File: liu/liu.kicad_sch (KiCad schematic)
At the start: 12 parts, among them J1 Screw Termial, J2 Screw Terminal, J5 I2C, J6 RotaryEncoder, U1 VoltageRegulator, U2 ESP32, U3 TJA1050

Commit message: added stuff
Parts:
- added D2: D, Resistor_THT:R_Axial_DIN0207_L6.3mm_D2.5mm_P10.16mm_Horizontal, symbol Device:D
- added R5: ~, Resistor_THT:R_Axial_DIN0207_L6.3mm_D2.5mm_P10.16mm_Horizontal, symbol Device:R
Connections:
- net 5V: now also D2.1 (K); no longer U1.4 (Pin_4)
- net at U2.1 (Pin_1): now also R5.1; no longer U3.2 (Pin_2)
- new net: D2.2 (A), U1.4 (Pin_4)
- new net: R5.2, U3.2 (Pin_2)

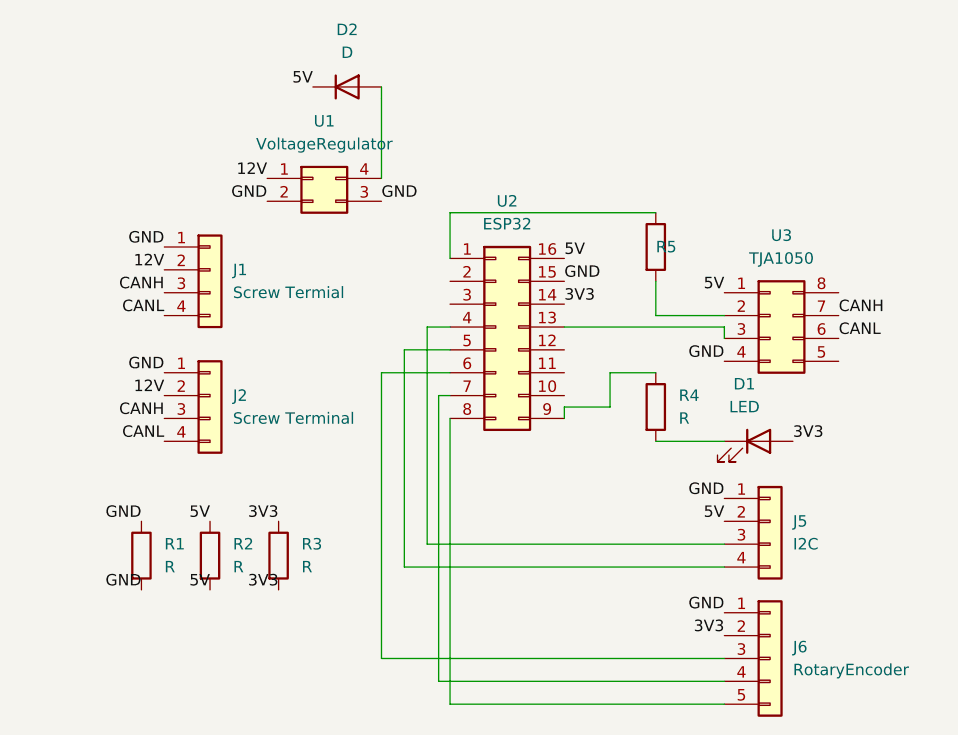
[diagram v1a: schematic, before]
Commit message: 4 screw terminals
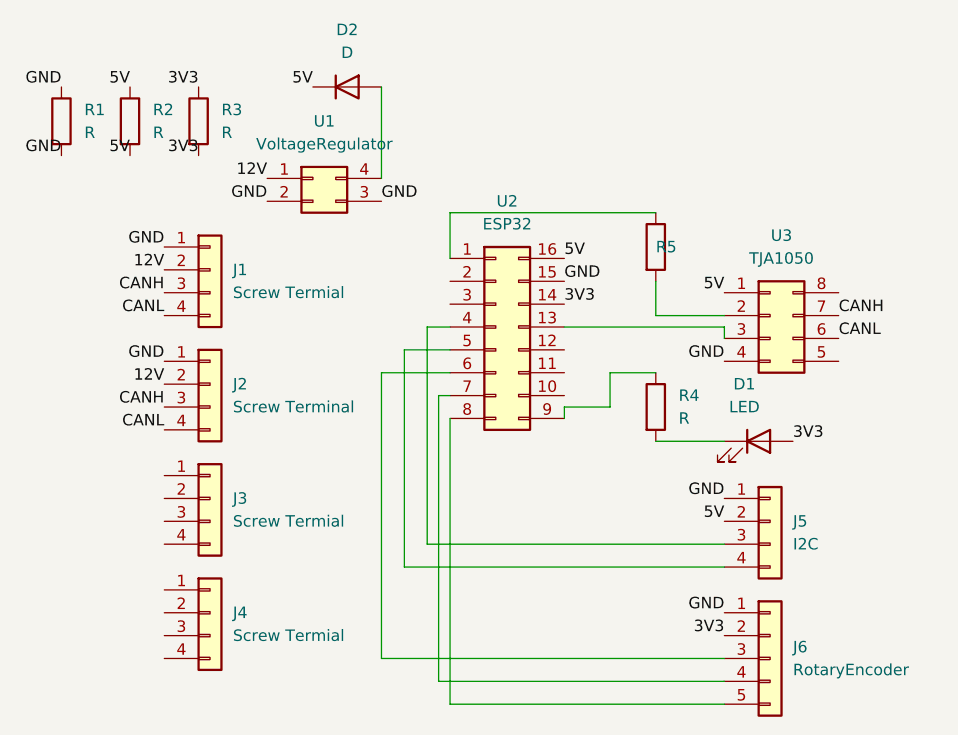
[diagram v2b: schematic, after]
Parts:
- added J3, J4: Screw Termial, Peabrain:ScrewTerminals_4P, symbol Connector_Generic:Conn_01x04
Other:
- moved on the sheet: J2, R1, R2, R3
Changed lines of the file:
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@@
+  (wire
+    (pts
+      (xy 78.74 27.94)
+      (xy 78.74 38.1)
+    )
+    (stroke
+      (width 0)
+      (type default)
+    )
+  )
   (wire
     (pts
@@
   )
   (label "5V"
-    (at 59.69 83.82 180)
+    (at 50.8 35.56 180)
     (effects
       (font
@@
   )
   (label "GND"
-    (at 52.07 83.82 180)
+    (at 43.18 35.56 180)
     (effects
       (font
@@
   )
   (label "CANL"
-    (at 54.61 67.31 180)
+    (at 54.61 66.04 180)
     (effects
       (font
@@
   )
   (label "3V3"
-    (at 67.31 83.82 180)
+    (at 58.42 35.56 180)
     (effects
       (font
@@
   )
   (label "12V"
-    (at 54.61 62.23 180)
+    (at 54.61 60.96 180)
     (effects
       (font
@@
   )
   (label "3V3"
-    (at 67.31 76.2 180)
+    (at 58.42 27.94 180)
     (effects
       (font
@@
   )
   (label "5V"
-    (at 59.69 76.2 180)
+    (at 50.8 27.94 180)
     (effects
       (font
@@
   )
   (label "GND"
-    (at 54.61 59.69 180)
+    (at 54.61 58.42 180)
     (effects
       (font
@@
   )
   (label "GND"
-    (at 52.07 76.2 180)
+    (at 43.18 27.94 180)
     (effects
       (font
@@
   )
   (label "CANH"
-    (at 54.61 64.77 180)
+    (at 54.61 63.5 180)
     (effects
       (font
@@
   (symbol
     (lib_id "Device:R")
-    (at 52.07 80.01 0)
+    (at 43.18 31.75 0)
     (unit 1)
     (exclude_from_sim no)
@@
     (fields_autoplaced yes)
     (property "Reference" "R1"
-      (at 54.61 78.7399 0)
+      (at 45.72 30.4799 0)
       (effects
         (font
@@
     )
     (property "Value" "R"
-      (at 54.61 81.2799 0)
+      (at 45.72 33.0199 0)
       (effects
         (font
@@
     )
     (property "Footprint" "Resistor_THT:R_Axial_DIN0207_L6.3mm_D2.5mm_P10.16mm_Horizontal"
-      (at 50.292 80.01 90)
+      (at 41.402 31.75 90)
       (effects
         (font
@@
     )
     (property "Datasheet" "~"
-      (at 52.07 80.01 0)
+      (at 43.18 31.75 0)
       (effects
         (font
@@
     )
     (property "Description" "Resistor"
-      (at 52.07 80.01 0)
+      (at 43.18 31.75 0)
       (effects
         (font
@@
   (symbol
     (lib_id "Device:R")
-    (at 59.69 80.01 0)
+    (at 50.8 31.75 0)
     (unit 1)
     (exclude_from_sim no)
@@
     (fields_autoplaced yes)
     (property "Reference" "R2"
-      (at 62.23 78.7399 0)
+      (at 53.34 30.4799 0)
       (effects
         (font
@@
     )
     (property "Value" "R"
-      (at 62.23 81.2799 0)
+      (at 53.34 33.0199 0)
       (effects
         (font
@@
     )
     (property "Footprint" "Resistor_THT:R_Axial_DIN0207_L6.3mm_D2.5mm_P10.16mm_Horizontal"
-      (at 57.912 80.01 90)
+      (at 49.022 31.75 90)
       (effects
         (font
@@
     )
     (property "Datasheet" "~"
-      (at 59.69 80.01 0)
+      (at 50.8 31.75 0)
       (effects
         (font
@@
     )
     (property "Description" "Resistor"
-      (at 59.69 80.01 0)
+      (at 50.8 31.75 0)
       (effects
         (font
@@
   (symbol
     (lib_id "Connector_Generic:Conn_01x04")
-    (at 59.69 62.23 0)
+    (at 59.69 73.66 0)
+    (unit 1)
+    (exclude_from_sim no)
+    (in_bom yes)
+    (on_board yes)
+    (dnp no)
+    (fields_autoplaced yes)
+    (property "Reference" "J3"
+      (at 62.23 73.6599 0)
+      (effects
+        (font
+          (size 1.27 1.27)
+        )
+        (justify left)
+      )
+    )
+    (property "Value" "Screw Termial"
+      (at 62.23 76.1999 0)
+      (effects
+        (font
+          (size 1.27 1.27)
+        )
+        (justify left)
+      )
+    )
+    (property "Footprint" "Peabrain:ScrewTerminals_4P"
+      (at 59.69 73.66 0)
+      (effects
+        (font
+          (size 1.27 1.27)
+        )
+        (hide yes)
+      )
+    )
+    (property "Datasheet" "~"
+      (at 59.69 73.66 0)
+      (effects
+        (font
+          (size 1.27 1.27)
+        )
+        (hide yes)
+      )
+    )
+    (property "Description" "Generic connector, single row, 01x04, script generated (kicad-library-utils/schlib/autogen/connector/)"
+      (at 59.69 73.66 0)
+      (effects
+        (font
+          (size 1.27 1.27)
+        )
+        (hide yes)
+      )
+    )
+    (pin "3"
+    )
+    (pin "2"
+    )
+    (pin "1"
+    )
+    (pin "4"
+    )
+    (instances
+      (project "liu"
+        (path "/94a9126b-1049-4434-a6c7-ce4492ba55c0"
+          (reference "J3")
+          (unit 1)
+        )
+      )
+    )
+  )
+  (symbol
+    (lib_id "Connector_Generic:Conn_01x04")
+    (at 59.69 60.96 0)
     (unit 1)
     (exclude_from_sim no)
@@
     (fields_autoplaced yes)
     (property "Reference" "J2"
-      (at 62.23 62.2299 0)
+      (at 62.23 60.9599 0)
       (effects
         (font
@@
     )
     (property "Value" "Screw Terminal"
-      (at 62.23 64.7699 0)
+      (at 62.23 63.4999 0)
       (effects
         (font
@@
     )
     (property "Footprint" "Peabrain:ScrewTerminals_4P"
-      (at 59.69 62.23 0)
+      (at 59.69 60.96 0)
       (effects
         (font
@@
     )
     (property "Datasheet" "~"
-      (at 59.69 62.23 0)
+      (at 59.69 60.96 0)
       (effects
         (font
@@
     )
     (property "Description" "Generic connector, single row, 01x04, script generated (kicad-library-utils/schlib/autogen/connector/)"
-      (at 59.69 62.23 0)
+      (at 59.69 60.96 0)
       (effects
         (font
@@
   )
   (symbol
+    (lib_id "Connector_Generic:Conn_01x04")
+    (at 59.69 86.36 0)
+    (unit 1)
+    (exclude_from_sim no)
+    (in_bom yes)
+    (on_board yes)
+    (dnp no)
+    (fields_autoplaced yes)
+    (property "Reference" "J4"
+      (at 62.23 86.3599 0)
+      (effects
+        (font
+          (size 1.27 1.27)
+        )
+        (justify left)
+      )
+    )
+    (property "Value" "Screw Termial"
+      (at 62.23 88.8999 0)
+      (effects
+        (font
+          (size 1.27 1.27)
+        )
+        (justify left)
+      )
+    )
+    (property "Footprint" "Peabrain:ScrewTerminals_4P"
+      (at 59.69 86.36 0)
+      (effects
+        (font
+          (size 1.27 1.27)
+        )
+        (hide yes)
+      )
+    )
+    (property "Datasheet" "~"
+      (at 59.69 86.36 0)
+      (effects
+        (font
+          (size 1.27 1.27)
+        )
+        (hide yes)
+      )
+    )
+    (property "Description" "Generic connector, single row, 01x04, script generated (kicad-library-utils/schlib/autogen/connector/)"
+      (at 59.69 86.36 0)
+      (effects
+        (font
+          (size 1.27 1.27)
+        )
+        (hide yes)
+      )
+    )
+    (pin "3"
+    )
+    (pin "2"
+    )
+    (pin "1"
+    )
+    (pin "4"
+    )
+    (instances
+      (project "liu"
+        (path "/94a9126b-1049-4434-a6c7-ce4492ba55c0"
+          (reference "J4")
+          (unit 1)
+        )
+      )
+    )
+  )
+  (symbol
     (lib_id "Device:R")
-    (at 67.31 80.01 0)
+    (at 58.42 31.75 0)
     (unit 1)
     (exclude_from_sim no)
@@
     (fields_autoplaced yes)
     (property "Reference" "R3"
-      (at 69.85 78.7399 0)
+      (at 60.96 30.4799 0)
       (effects
         (font
@@
     )
     (property "Value" "R"
-      (at 69.85 81.2799 0)
+      (at 60.96 33.0199 0)
       (effects
         (font
@@
     )
     (property "Footprint" "Resistor_THT:R_Axial_DIN0207_L6.3mm_D2.5mm_P10.16mm_Horizontal"
-      (at 65.532 80.01 90)
+      (at 56.642 31.75 90)
       (effects
         (font
@@
     )
     (property "Datasheet" "~"
-      (at 67.31 80.01 0)
+      (at 58.42 31.75 0)
       (effects
         (font
@@
     )
     (property "Description" "Resistor"
-      (at 67.31 80.01 0)
+      (at 58.42 31.75 0)
       (effects
         (font
@@
     )
   )
-  (wire
-    (pts
-      (xy 78.74000000000001 27.94)
-      (xy 78.74 29.21)
-    )
-    (stroke
-      (width 0)
-      (type default)
-    )
-  )
-  (wire
-    (pts
-      (xy 78.74 29.21)
-      (xy 78.74 38.1)
-    )
-    (stroke
-      (width 0)
-      (type default)
-    )
-  )
